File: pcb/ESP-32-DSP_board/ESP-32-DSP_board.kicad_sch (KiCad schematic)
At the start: 56 parts, among them J1 USB_C_Receptacle_USB2.0, J2 Conn_01x04_Pin, J3 Conn_01x04_Pin, J4 Conn_01x07_Pin, J5 Conn_01x07_Pin, Q1 BC847, Q2 BC847, U1 AZ1117IH-3.3, U2 ESP32-WROOM-32UE-N8, U3 USBLC6-2P6, U4 CP2104, U5 ADS8688

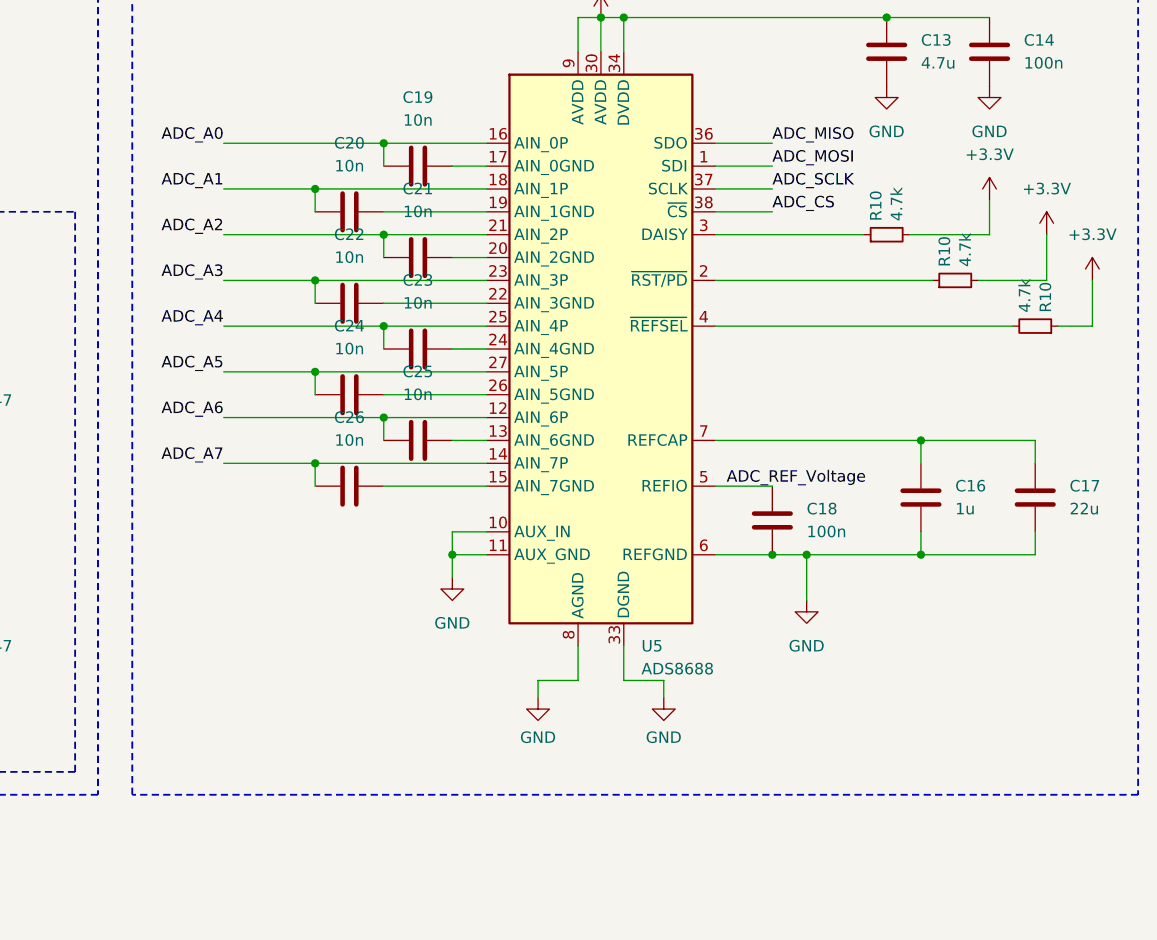
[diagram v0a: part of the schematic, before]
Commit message: Separated GND and GNDA
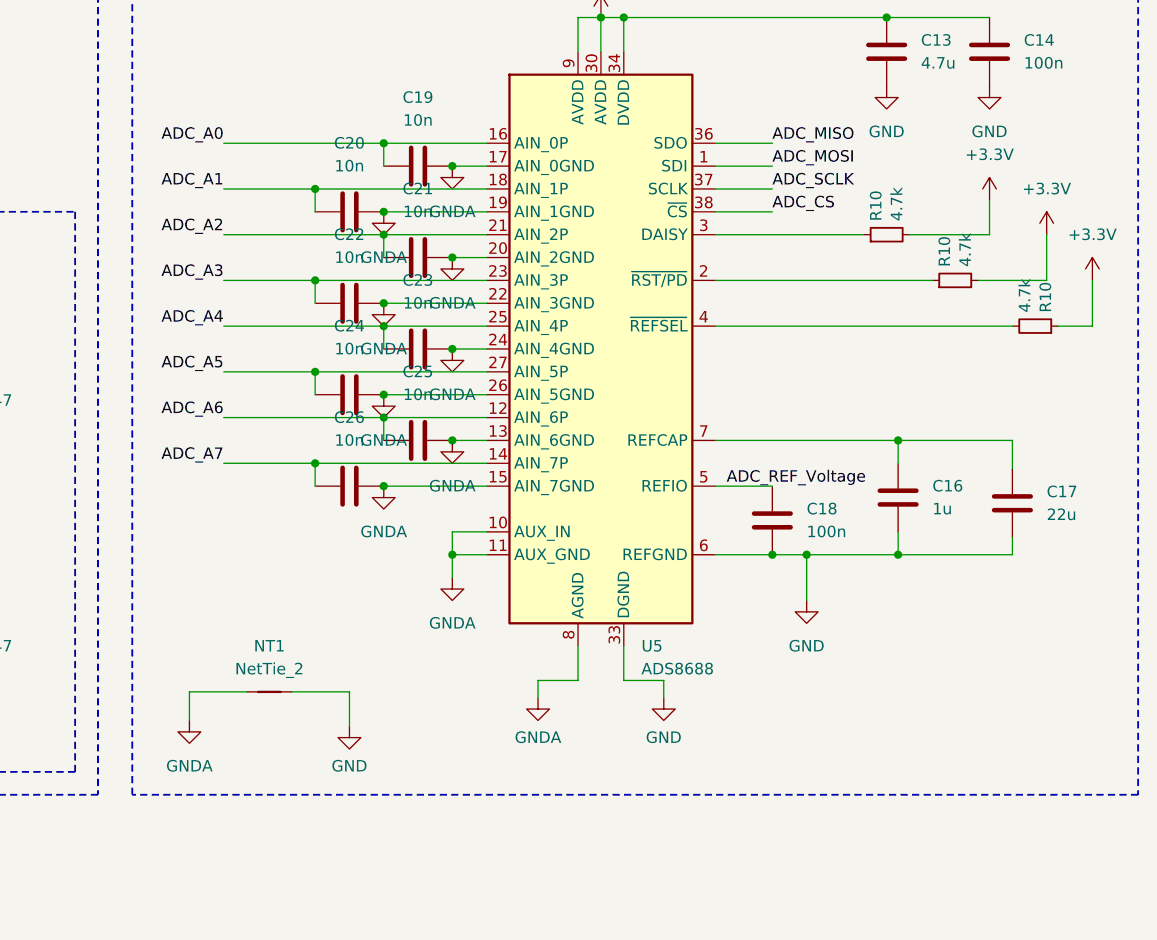
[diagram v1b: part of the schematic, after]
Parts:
- added NT1: NetTie_2, NetTie:NetTie-2_THT_Pad1.0mm, symbol Device:NetTie_2
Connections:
- net GND: now also NT1.2; no longer U5.10 (AUX_IN), U5.11 (AUX_GND), U5.28 (AGND), U5.29 (AGND), U5.31 (AGND), U5.32 (AGND), U5.8 (AGND)
- net GNDA: now reaches C24.1, U5.26 (AIN_5GND)
- net GNDA: now also C19.2, C20.2, C21.1, C22.1, C23.1, C25.2, C26.1, U5.10 (AUX_IN), U5.11 (AUX_GND), U5.13 (AIN_6GND), U5.15 (AIN_7GND), U5.17 (AIN_0GND), U5.19 (AIN_1GND), U5.20 (AIN_2GND), U5.22 (AIN_3GND), U5.24 (AIN_4GND), U5.28 (AGND), U5.29 (AGND), U5.31 (AGND), U5.32 (AGND), U5.8 (AGND), NT1.1
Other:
- moved on the sheet: C16, C17

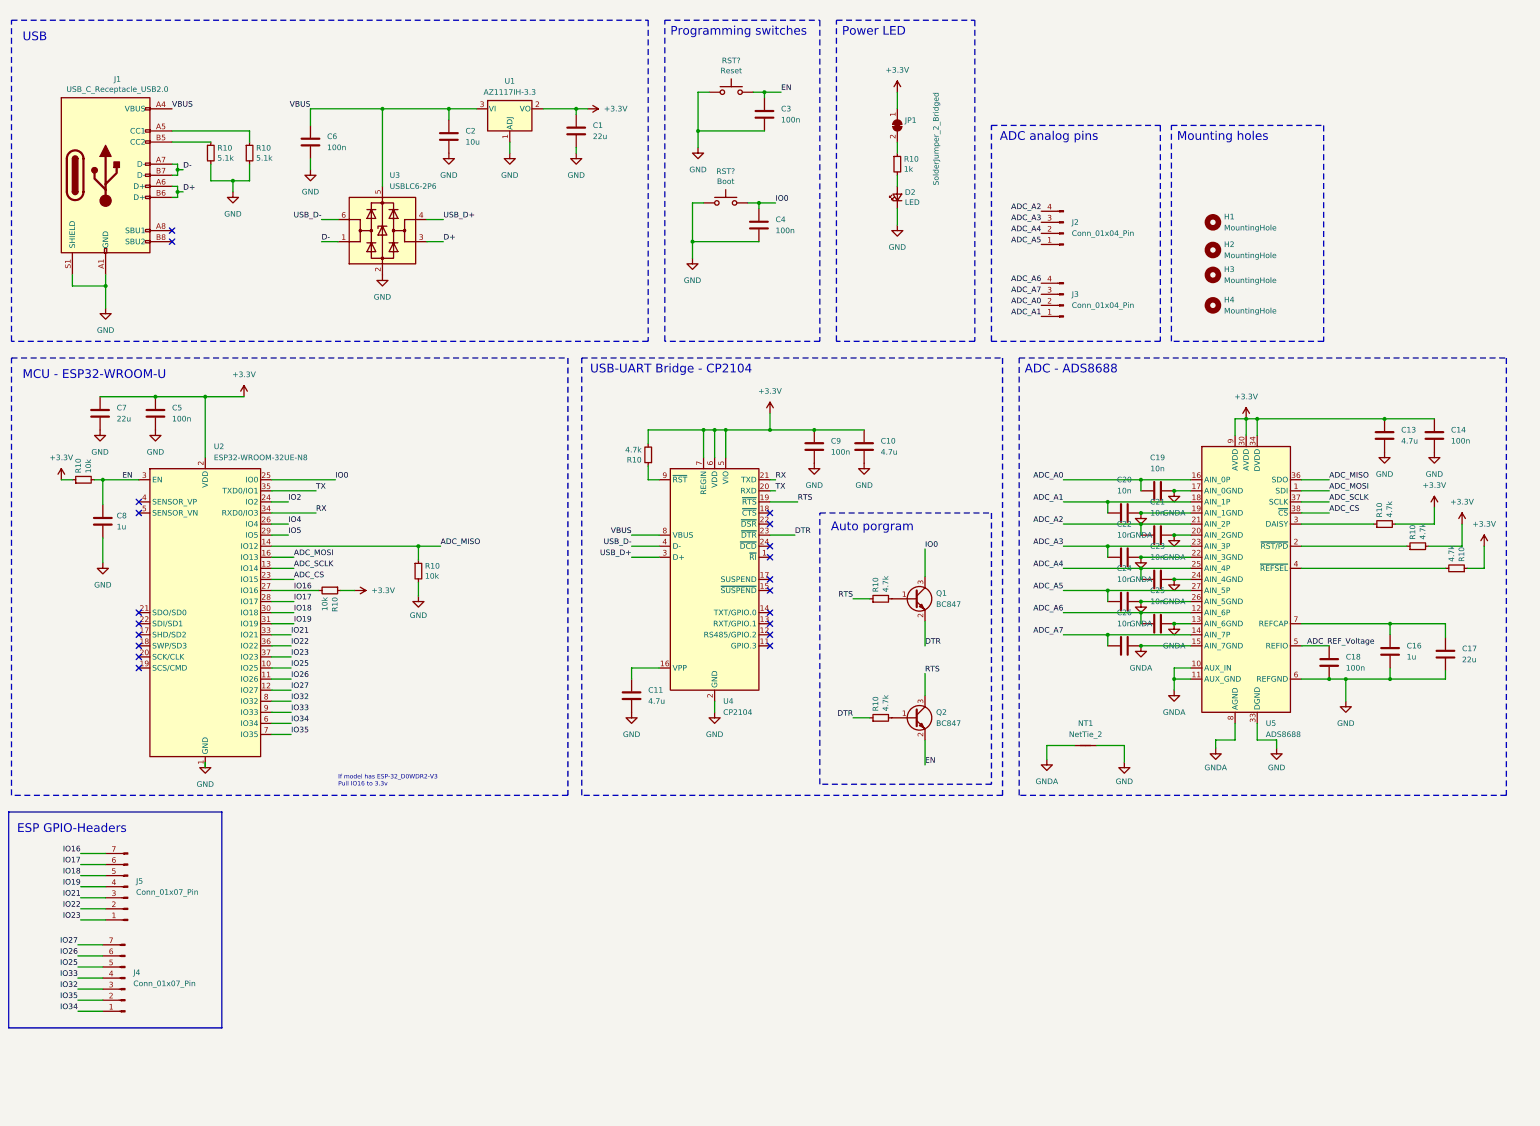
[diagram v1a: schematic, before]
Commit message: Updated ADC configutation
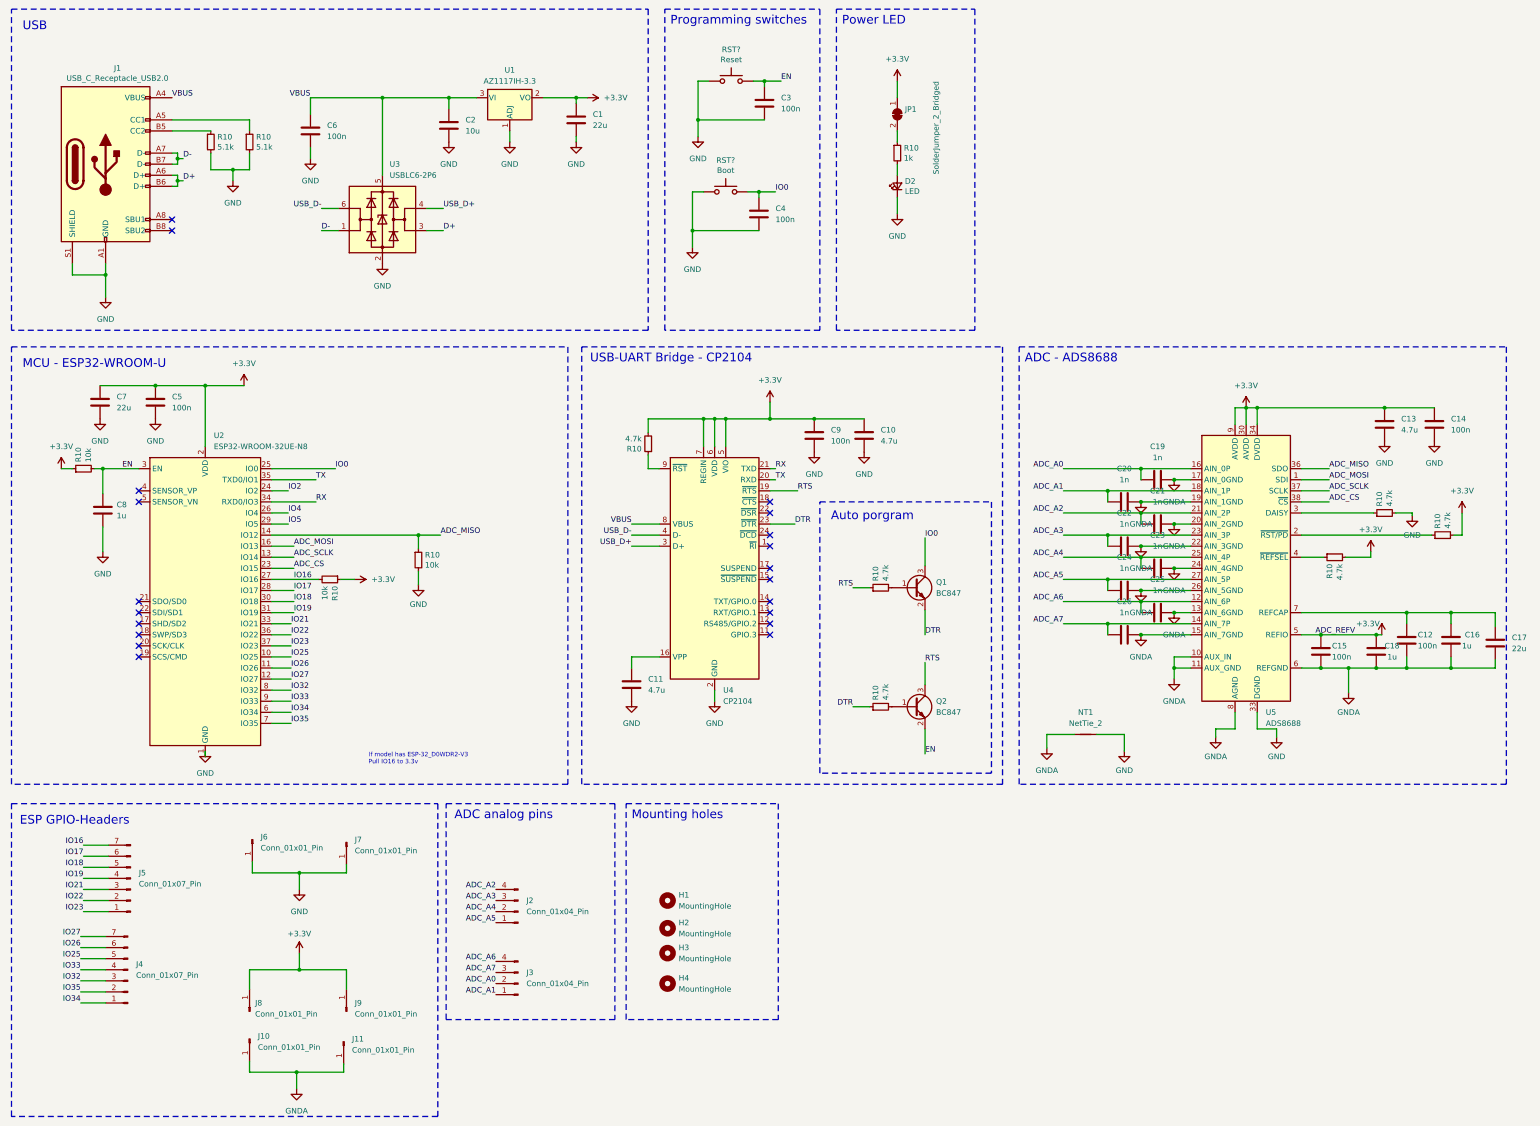
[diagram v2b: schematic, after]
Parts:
- added C12, C15: 100n, Capacitor_SMD:C_0402_1005Metric, symbol Device:C
- added J10, J11, J6, J7, J8, J9: Conn_01x01_Pin, Connector_PinSocket_2.00mm:PinSocket_1x01_P2.00mm_Vertical, symbol Connector:Conn_01x01_Pin
- C18: value 100n -> 1u; footprint Capacitor_SMD:C_0402_1005Metric -> Capacitor_SMD:C_0603_1608Metric
- C19, C20, C21, C22, C23, C24, C25, C26: value 10n -> 1n
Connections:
- net ADC_REF_Voltage is gone; now on net +3.3V: C18.1, U5.5 (REFIO)
- net +3.3V: now also R10.2, C15.2, J8.1 (Pin_1), J9.1 (Pin_1); no longer R10.1, R10.2
- net GND: now also R10.2, J6.1 (Pin_1), J7.1 (Pin_1); no longer C16.2, C17.2, C18.2, U5.6 (REFGND)
- net GNDA: now also C16.2, C17.2, C18.2, U5.6 (REFGND), C12.1, C15.1, J10.1 (Pin_1), J11.1 (Pin_1)
- net at C16.1, C17.1, U5.7 (REFCAP): now also C12.2
- net at U5.4 (~{REFSEL}): now also R10.1; no longer R10.2
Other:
- moved on the sheet: C1, C10, C11, C13, C14, C16, C17, C19, C2, C20, C21, C22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
